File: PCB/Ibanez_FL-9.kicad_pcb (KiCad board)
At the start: 2 copper layers, 50.8 x 22.9 mm, 38 parts, among them J1 SENSOR_UART-QT, J2 PWR_IN, J6 MOTOR_OUT, M1 Feather_M4_Express, Q1 DMG2301L, U1 INA260, U2 DRV8830

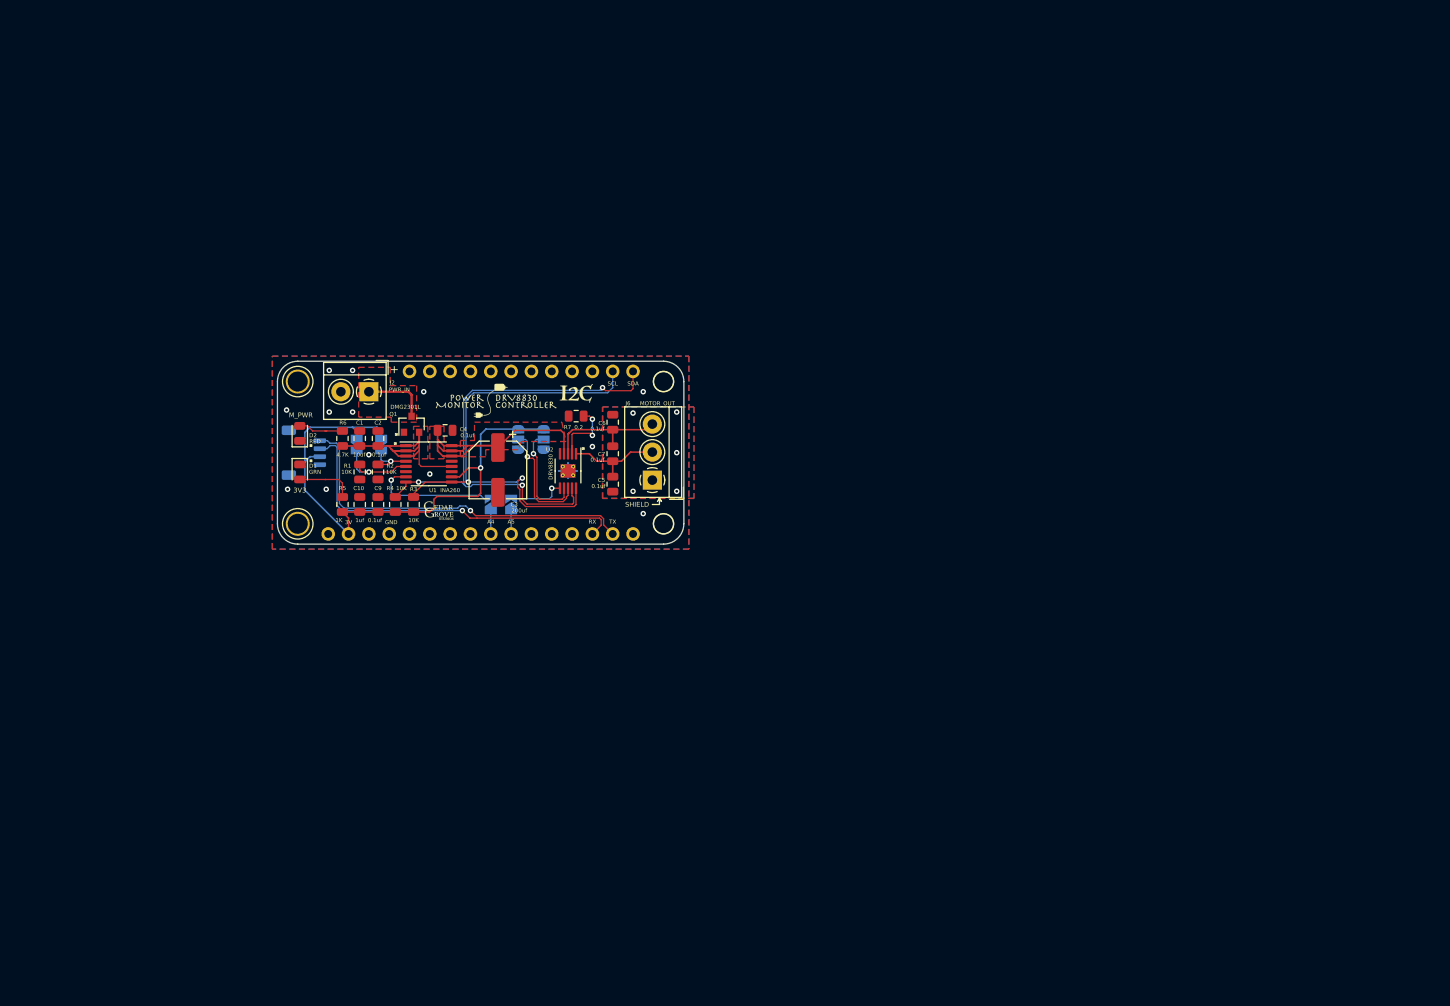
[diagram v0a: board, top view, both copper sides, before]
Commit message: update docs; correct component labels and footprints
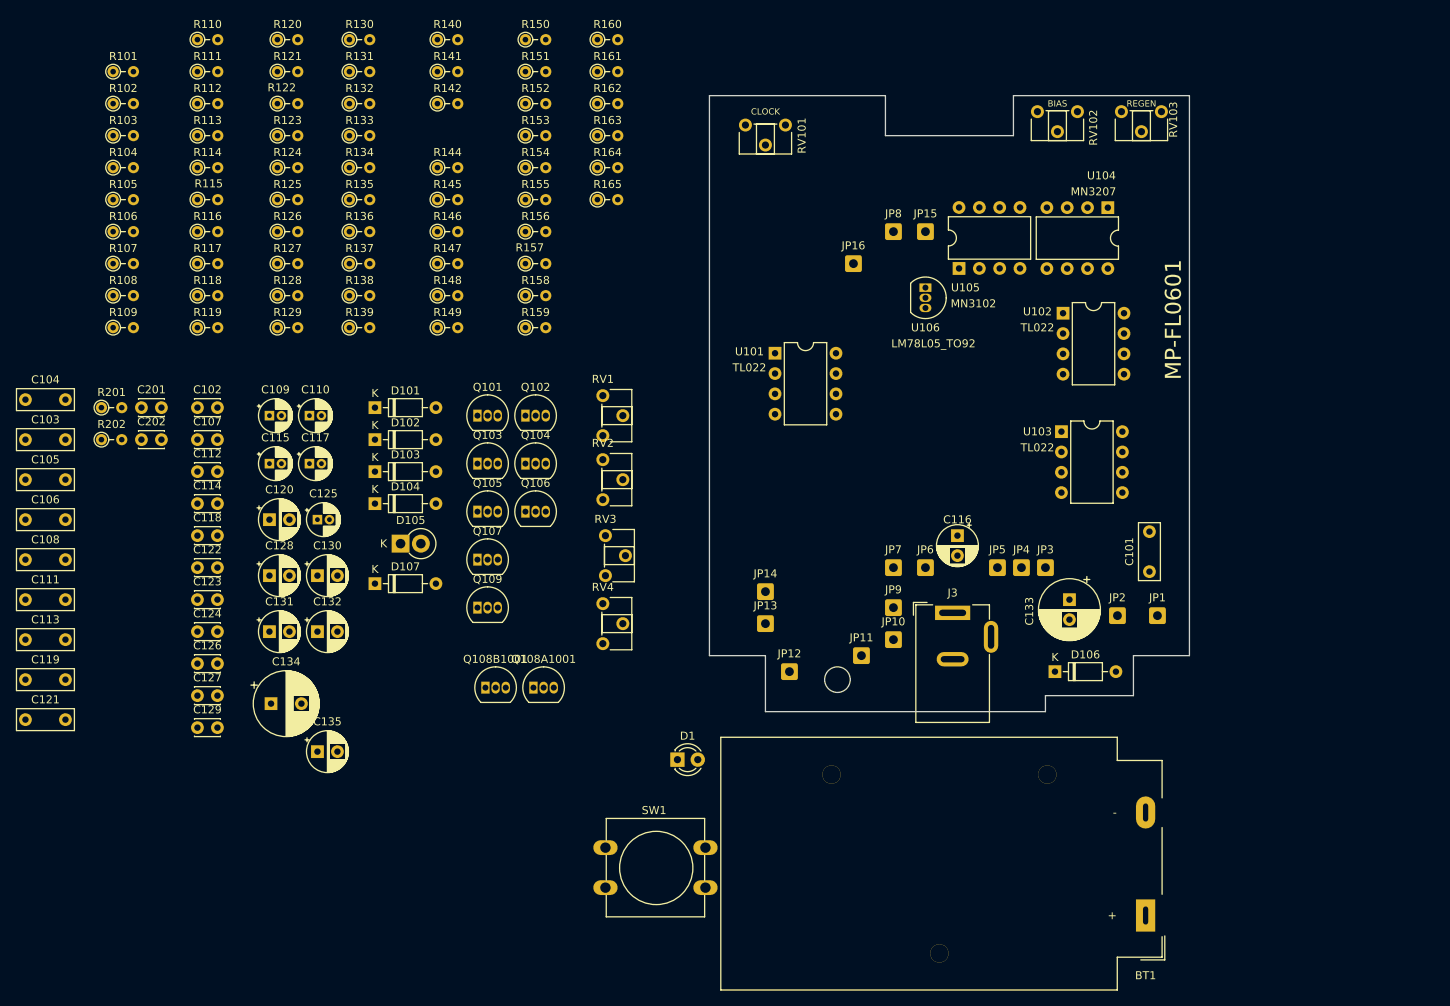
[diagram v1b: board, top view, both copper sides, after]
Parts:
- removed C1: 10uf, Capacitor_SMD:C_0805_2012Metric
- removed C10: 1uf, Capacitor_SMD:C_0805_2012Metric
- removed C2, C4, C5, C6, C7, C9: 0.1uf, Capacitor_SMD:C_0805_2012Metric
- removed C3: 200uf, Capacitor_SMD:CP_Elec_6.6x6.6
- removed D2: RED, LED_SMD:LED_0805_2012Metric
- removed G***: CedarGroveStudios_TEXT_LOGO_4x2_7mm, Adafruit:CedarGroveStudios_TEXT_LOGO_4x2_7mm
- removed G*** (x2): LOGO, Adafruit:mtc_wing_DRV8830_24x14mm
- removed G*** (x2): LOGO, Adafruit:I2C_LOGO
- removed G***: Feather_LOGO_8x4mm, Adafruit:Feather_LOGO_8x4mm
- removed G***: LOGO, Adafruit:CedarGroveStudios_TEXT_LOGO_8x5_4mm
- removed J1: SENSOR_UART-QT, Connector_JST:JST_SH_SM04B-SRSS-TB_1x04-1MP_P1.00mm_Horizontal
- removed J2: PWR_IN, TerminalBlock_4Ucon:TerminalBlock_4Ucon_1x02_P3.50mm_Horizontal
- removed J6: MOTOR_OUT, TerminalBlock_4Ucon:TerminalBlock_4Ucon_1x03_P3.50mm_Horizontal
- removed M1: Feather_M4_Express, Adafruit:Adafruit_Feather_M4_Express_bare
- removed Q1: DMG2301L, Package_TO_SOT_SMD:SOT-23
- removed R1, R2, R3, R4: 10K, Resistor_SMD:R_0805_2012Metric
- removed R5: 1K, Resistor_SMD:R_0805_2012Metric
- removed R6: 4.7K, Resistor_SMD:R_0805_2012Metric
- removed R7: 0.2, Resistor_SMD:R_0805_2012Metric
- removed U1: INA260, Package_SO:TSSOP-16_4.4x5mm_P0.65mm
- removed U2: DRV8830, Package_SO:MSOP-10-1EP_3x3mm_P0.5mm_EP1.68x1.88mm_ThermalVias
- added BT1: 9V Battery, Battery:BatteryHolder_MPD_BA9VPC_1xPP3, F.Cu at (235.5, 145.5)
- added C101: 0.047uf FILM, Capacitor_THT:C_Rect_L7.0mm_W2.5mm_P5.00mm, F.Cu at (236.0, 102.5)
- added C102: 100pf CER, Capacitor_THT:C_Disc_D3.0mm_W2.0mm_P2.50mm, F.Cu at (117.0, 82.0)
- added C103: 0.022uf FILM, Capacitor_THT:C_Rect_L7.0mm_W2.5mm_P5.00mm, F.Cu at (95.5, 86.0)
- added C104: 0.047uf FILM, Capacitor_THT:C_Rect_L7.0mm_W2.5mm_P5.00mm, F.Cu at (95.5, 81.0)
- added C105: 0.004uf FILM, Capacitor_THT:C_Rect_L7.0mm_W2.5mm_P5.00mm, F.Cu at (95.5, 91.0)
- added C106: 0.01uf FILM, Capacitor_THT:C_Rect_L7.0mm_W2.5mm_P5.00mm, F.Cu at (95.5, 96.0)
- added C107: 120pf CER, Capacitor_THT:C_Disc_D3.0mm_W2.0mm_P2.50mm, F.Cu at (117.0, 86.0)
- added C108: 0.033uf FILM, Capacitor_THT:C_Rect_L7.0mm_W2.5mm_P5.00mm, F.Cu at (95.5, 101.0)
- added C109: 1uf/50v, Capacitor_THT:CP_Radial_D4.0mm_P1.50mm, F.Cu at (126.0, 83.0)
- added C110: 1uf/50, Capacitor_THT:CP_Radial_D4.0mm_P1.50mm, F.Cu at (131.0, 83.0)
- added C111: 0.0015uf FILM, Capacitor_THT:C_Rect_L7.0mm_W2.5mm_P5.00mm, F.Cu at (95.5, 106.0)
- added C112: 0.001uf CER, Capacitor_THT:C_Disc_D3.0mm_W2.0mm_P2.50mm, F.Cu at (117.0, 90.0)
- added C113: 0.003uf FILM, Capacitor_THT:C_Rect_L7.0mm_W2.5mm_P5.00mm, F.Cu at (95.5, 111.0)
- added C114: 560pf CER, Capacitor_THT:C_Disc_D3.0mm_W2.0mm_P2.50mm, F.Cu at (117.0, 94.0)
- added C115: 1uf/50, Capacitor_THT:CP_Radial_D4.0mm_P1.50mm, F.Cu at (126.0, 89.0)
- added C116: 0.22uf/50v, Capacitor_THT:CP_Radial_D5.0mm_P2.50mm, F.Cu at (212.0, 98.0)
- added C117: 1uf/50, Capacitor_THT:CP_Radial_D4.0mm_P1.50mm, F.Cu at (131.0, 89.0)
- added C118: 100pf CER, Capacitor_THT:C_Disc_D3.0mm_W2.0mm_P2.50mm, F.Cu at (117.0, 98.0)
- added C119: 0.004 FILM, Capacitor_THT:C_Rect_L7.0mm_W2.5mm_P5.00mm, F.Cu at (95.5, 116.0)
- added C120: 10uf/16v, Capacitor_THT:CP_Radial_D5.0mm_P2.50mm, F.Cu at (126.0, 96.0)
- added C121: 0.047uf FILM, Capacitor_THT:C_Rect_L7.0mm_W2.5mm_P5.00mm, F.Cu at (95.5, 121.0)
- added C122: 1000pf CER, Capacitor_THT:C_Disc_D3.0mm_W2.0mm_P2.50mm, F.Cu at (117.0, 102.0)
- added C123: 1000pf CER, Capacitor_THT:C_Disc_D3.0mm_W2.0mm_P2.50mm, F.Cu at (117.0, 106.0)
- added C124: 1000pf CER, Capacitor_THT:C_Disc_D3.0mm_W2.0mm_P2.50mm, F.Cu at (117.0, 110.0)
- added C125: 1uf/50v, Capacitor_THT:CP_Radial_D4.0mm_P1.50mm, F.Cu at (132.0, 96.0)
- added C126: 20pf CER, Capacitor_THT:C_Disc_D3.0mm_W2.0mm_P2.50mm, F.Cu at (117.0, 114.0)
- added C127: 5pf CER, Capacitor_THT:C_Disc_D3.0mm_W2.0mm_P2.50mm, F.Cu at (117.0, 118.0)
- added C128: 22uf/10v, Capacitor_THT:CP_Radial_D5.0mm_P2.50mm, F.Cu at (126.0, 103.0)
- added C129: 0.01uf, Capacitor_THT:C_Disc_D3.0mm_W2.0mm_P2.50mm, F.Cu at (117.0, 122.0)
- added C130: 47uf/10v, Capacitor_THT:CP_Radial_D5.0mm_P2.50mm, F.Cu at (132.0, 103.0)
- added C131: 47uf/10v, Capacitor_THT:CP_Radial_D5.0mm_P2.50mm, F.Cu at (126.0, 110.0)
- added C132: 47uf/6.3v, Capacitor_THT:CP_Radial_D5.0mm_P2.50mm, F.Cu at (132.0, 110.0)
- added C133: 100uf/16v, Capacitor_THT:CP_Radial_D7.5mm_P2.50mm, F.Cu at (226.0, 106.0)
- added C134: 100uf/10v, Capacitor_THT:CP_Radial_D8.0mm_P3.80mm, F.Cu at (126.2, 119.0)
- added C135: 47uf/6.3v, Capacitor_THT:CP_Radial_D5.0mm_P2.50mm, F.Cu at (132.0, 125.0)
- added C201: 0.001uf CER, Capacitor_THT:C_Disc_D3.0mm_W2.0mm_P2.50mm, F.Cu at (110.0, 82.0)
- added C202: 0.001uf CER, Capacitor_THT:C_Disc_D3.0mm_W2.0mm_P2.50mm, F.Cu at (110.0, 86.0)
- added D101: 1N4004, Diode_THT:D_DO-35_SOD27_P7.62mm_Horizontal, F.Cu at (139.2, 82.0)
- added D102: 1N4004, Diode_THT:D_DO-35_SOD27_P7.62mm_Horizontal, F.Cu at (139.2, 86.0)
- added D103: 1N4004, Diode_THT:D_DO-35_SOD27_P7.62mm_Horizontal, F.Cu at (139.2, 90.0)
- added D104: 1N4004, Diode_THT:D_DO-35_SOD27_P7.62mm_Horizontal, F.Cu at (139.2, 94.0)
- added D105: RD5.1EB, Diode_THT:D_DO-15_P2.54mm_Vertical_KathodeUp, F.Cu at (142.4, 99.0)
- added D106: W05C, Diode_THT:D_DO-35_SOD27_P7.62mm_Horizontal, F.Cu at (224.2, 115.0)
- added D107: 1N4004, Diode_THT:D_DO-35_SOD27_P7.62mm_Horizontal, F.Cu at (139.2, 104.0)
- added J3: EXT_DC, Connector_BarrelJack:BarrelJack_Wuerth_6941xx301002, F.Cu at (211.4, 107.7)
- added JP10: BLK, Connector_Wire:SolderWire-0.5sqmm_1x01_D0.9mm_OD2.1mm, F.Cu at (204.0, 111.0)
- added JP11: W/R, Connector_Wire:SolderWire-0.5sqmm_1x01_D0.9mm_OD2.1mm, F.Cu at (200.0, 113.0)
- added JP12: PINK, Connector_Wire:SolderWire-0.5sqmm_1x01_D0.9mm_OD2.1mm, F.Cu at (191.0, 115.0)
- added JP13: GRN, Connector_Wire:SolderWire-0.5sqmm_1x01_D0.9mm_OD2.1mm, F.Cu at (188.0, 109.0)
- added JP14: ORA, Connector_Wire:SolderWire-0.5sqmm_1x01_D0.9mm_OD2.1mm, F.Cu at (188.0, 105.0)
- added JP15: RED, Connector_Wire:SolderWire-0.5sqmm_1x01_D0.9mm_OD2.1mm, F.Cu at (208.0, 60.0)
- added JP16: Y-GR, Connector_Wire:SolderWire-0.5sqmm_1x01_D0.9mm_OD2.1mm, F.Cu at (199.0, 64.0)
- added JP7: BRN, Connector_Wire:SolderWire-0.5sqmm_1x01_D0.9mm_OD2.1mm, F.Cu at (204.0, 102.0)
- added JP8: S-BL, Connector_Wire:SolderWire-0.5sqmm_1x01_D0.9mm_OD2.1mm, F.Cu at (204.0, 60.0)
- added JP9: RED, Connector_Wire:SolderWire-0.5sqmm_1x01_D0.9mm_OD2.1mm, F.Cu at (204.0, 107.0)
- added Q101: 2SC2458GR, Package_TO_SOT_THT:TO-92_Inline, F.Cu at (152.0, 83.0)
- added Q102: 2SC2458GR, Package_TO_SOT_THT:TO-92_Inline, F.Cu at (158.0, 83.0)
- added Q103: 2SK44SPC, Package_TO_SOT_THT:TO-92_Inline, F.Cu at (152.0, 89.0)
- added Q104: 2SC2458GR, Package_TO_SOT_THT:TO-92_Inline, F.Cu at (158.0, 89.0)
- added Q105: 2SC2458GR, Package_TO_SOT_THT:TO-92_Inline, F.Cu at (152.0, 95.0)
- added Q106: 2SC2458GR, Package_TO_SOT_THT:TO-92_Inline, F.Cu at (158.0, 95.0)
- added Q107: 2SA1048Y/GR, Package_TO_SOT_THT:TO-92_Inline, F.Cu at (152.0, 101.0)
- added Q108A1001: 2SC1583F, Package_TO_SOT_THT:TO-92_Inline, F.Cu at (159.0, 117.0)
- added Q108B1001: 2SC1583F, Package_TO_SOT_THT:TO-92_Inline, F.Cu at (153.0, 117.0)
- added Q109: 2SC2458GR, Package_TO_SOT_THT:TO-92_Inline, F.Cu at (152.0, 107.0)
- added R101: 1K, Resistor_THT:R_Axial_DIN0204_L3.6mm_D1.6mm_P2.54mm_Vertical, F.Cu at (106.5, 40.0)
- added R102: 510K, Resistor_THT:R_Axial_DIN0204_L3.6mm_D1.6mm_P2.54mm_Vertical, F.Cu at (106.5, 44.0)
- added R103: 91K, Resistor_THT:R_Axial_DIN0204_L3.6mm_D1.6mm_P2.54mm_Vertical, F.Cu at (106.5, 48.0)
- added R104: 18K, Resistor_THT:R_Axial_DIN0204_L3.6mm_D1.6mm_P2.54mm_Vertical, F.Cu at (106.5, 52.0)
- added R105: 180K, Resistor_THT:R_Axial_DIN0204_L3.6mm_D1.6mm_P2.54mm_Vertical, F.Cu at (106.5, 56.0)
- added R106: 510K, Resistor_THT:R_Axial_DIN0204_L3.6mm_D1.6mm_P2.54mm_Vertical, F.Cu at (106.5, 60.0)
- added R107: 100K, Resistor_THT:R_Axial_DIN0204_L3.6mm_D1.6mm_P2.54mm_Vertical, F.Cu at (106.5, 64.0)
- added R108: 10K, Resistor_THT:R_Axial_DIN0204_L3.6mm_D1.6mm_P2.54mm_Vertical, F.Cu at (106.5, 68.0)
- added R109: 47K, Resistor_THT:R_Axial_DIN0204_L3.6mm_D1.6mm_P2.54mm_Vertical, F.Cu at (106.5, 72.0)
- added R110: 12K, Resistor_THT:R_Axial_DIN0204_L3.6mm_D1.6mm_P2.54mm_Vertical, F.Cu at (117.0, 36.0)
- added R111: 12K, Resistor_THT:R_Axial_DIN0204_L3.6mm_D1.6mm_P2.54mm_Vertical, F.Cu at (117.0, 40.0)
- added R112: 10K, Resistor_THT:R_Axial_DIN0204_L3.6mm_D1.6mm_P2.54mm_Vertical, F.Cu at (117.0, 44.0)
- added R113: 100K, Resistor_THT:R_Axial_DIN0204_L3.6mm_D1.6mm_P2.54mm_Vertical, F.Cu at (117.0, 48.0)
- added R114: 5.1K, Resistor_THT:R_Axial_DIN0204_L3.6mm_D1.6mm_P2.54mm_Vertical, F.Cu at (117.0, 52.0)
- added R115: 5.1K, Resistor_THT:R_Axial_DIN0204_L3.6mm_D1.6mm_P2.54mm_Vertical, F.Cu at (117.0, 56.0)
- added R116: 56K, Resistor_THT:R_Axial_DIN0204_L3.6mm_D1.6mm_P2.54mm_Vertical, F.Cu at (117.0, 60.0)
- added R117: 18K, Resistor_THT:R_Axial_DIN0204_L3.6mm_D1.6mm_P2.54mm_Vertical, F.Cu at (117.0, 64.0)
- added R118: 18K, Resistor_THT:R_Axial_DIN0204_L3.6mm_D1.6mm_P2.54mm_Vertical, F.Cu at (117.0, 68.0)
- added R119: 18K, Resistor_THT:R_Axial_DIN0204_L3.6mm_D1.6mm_P2.54mm_Vertical, F.Cu at (117.0, 72.0)
- added R120: 10K, Resistor_THT:R_Axial_DIN0204_L3.6mm_D1.6mm_P2.54mm_Vertical, F.Cu at (127.0, 36.0)
- added R121: 13K, Resistor_THT:R_Axial_DIN0204_L3.6mm_D1.6mm_P2.54mm_Vertical, F.Cu at (127.0, 40.0)
- added R122: 13K, Resistor_THT:R_Axial_DIN0204_L3.6mm_D1.6mm_P2.54mm_Vertical, F.Cu at (127.0, 44.0)
- added R123: 10K, Resistor_THT:R_Axial_DIN0204_L3.6mm_D1.6mm_P2.54mm_Vertical, F.Cu at (127.0, 48.0)
- added R124: 100K, Resistor_THT:R_Axial_DIN0204_L3.6mm_D1.6mm_P2.54mm_Vertical, F.Cu at (127.0, 52.0)
- added R125: 100K, Resistor_THT:R_Axial_DIN0204_L3.6mm_D1.6mm_P2.54mm_Vertical, F.Cu at (127.0, 56.0)
- added R126: 51K, Resistor_THT:R_Axial_DIN0204_L3.6mm_D1.6mm_P2.54mm_Vertical, F.Cu at (127.0, 60.0)
- added R127: 91K, Resistor_THT:R_Axial_DIN0204_L3.6mm_D1.6mm_P2.54mm_Vertical, F.Cu at (127.0, 64.0)
- added R128: 18K, Resistor_THT:R_Axial_DIN0204_L3.6mm_D1.6mm_P2.54mm_Vertical, F.Cu at (127.0, 68.0)
- added R129: 91K, Resistor_THT:R_Axial_DIN0204_L3.6mm_D1.6mm_P2.54mm_Vertical, F.Cu at (127.0, 72.0)
- added R130: 10K, Resistor_THT:R_Axial_DIN0204_L3.6mm_D1.6mm_P2.54mm_Vertical, F.Cu at (136.0, 36.0)
- added R131: 470, Resistor_THT:R_Axial_DIN0204_L3.6mm_D1.6mm_P2.54mm_Vertical, F.Cu at (136.0, 40.0)
- added R132: 100K, Resistor_THT:R_Axial_DIN0204_L3.6mm_D1.6mm_P2.54mm_Vertical, F.Cu at (136.0, 44.0)
- added R133: 1M, Resistor_THT:R_Axial_DIN0204_L3.6mm_D1.6mm_P2.54mm_Vertical, F.Cu at (136.0, 48.0)
- added R134: 10K, Resistor_THT:R_Axial_DIN0204_L3.6mm_D1.6mm_P2.54mm_Vertical, F.Cu at (136.0, 52.0)
- added R135: 10K, Resistor_THT:R_Axial_DIN0204_L3.6mm_D1.6mm_P2.54mm_Vertical, F.Cu at (136.0, 56.0)
- added R136: 56K, Resistor_THT:R_Axial_DIN0204_L3.6mm_D1.6mm_P2.54mm_Vertical, F.Cu at (136.0, 60.0)
- added R137: 56K, Resistor_THT:R_Axial_DIN0204_L3.6mm_D1.6mm_P2.54mm_Vertical, F.Cu at (136.0, 64.0)
- added R138: 1M, Resistor_THT:R_Axial_DIN0204_L3.6mm_D1.6mm_P2.54mm_Vertical, F.Cu at (136.0, 68.0)
- added R139: 62K, Resistor_THT:R_Axial_DIN0204_L3.6mm_D1.6mm_P2.54mm_Vertical, F.Cu at (136.0, 72.0)
- added R140: 22K, Resistor_THT:R_Axial_DIN0204_L3.6mm_D1.6mm_P2.54mm_Vertical, F.Cu at (147.0, 36.0)
- added R141: 22, Resistor_THT:R_Axial_DIN0204_L3.6mm_D1.6mm_P2.54mm_Vertical, F.Cu at (147.0, 40.0)
- added R142: 100, Resistor_THT:R_Axial_DIN0204_L3.6mm_D1.6mm_P2.54mm_Vertical, F.Cu at (147.0, 44.0)
- added R144: 2.2K, Resistor_THT:R_Axial_DIN0204_L3.6mm_D1.6mm_P2.54mm_Vertical, F.Cu at (147.0, 52.0)
- added R145: 330, Resistor_THT:R_Axial_DIN0204_L3.6mm_D1.6mm_P2.54mm_Vertical, F.Cu at (147.0, 56.0)
- added R146: 33K, Resistor_THT:R_Axial_DIN0204_L3.6mm_D1.6mm_P2.54mm_Vertical, F.Cu at (147.0, 60.0)
- added R147: 27K, Resistor_THT:R_Axial_DIN0204_L3.6mm_D1.6mm_P2.54mm_Vertical, F.Cu at (147.0, 64.0)
- added R148: 10K, Resistor_THT:R_Axial_DIN0204_L3.6mm_D1.6mm_P2.54mm_Vertical, F.Cu at (147.0, 68.0)
- added R149: 9.1K, Resistor_THT:R_Axial_DIN0204_L3.6mm_D1.6mm_P2.54mm_Vertical, F.Cu at (147.0, 72.0)
- added R150: 2.2M, Resistor_THT:R_Axial_DIN0204_L3.6mm_D1.6mm_P2.54mm_Vertical, F.Cu at (158.0, 36.0)
- added R151: 150K, Resistor_THT:R_Axial_DIN0204_L3.6mm_D1.6mm_P2.54mm_Vertical, F.Cu at (158.0, 40.0)
- added R152: 220K, Resistor_THT:R_Axial_DIN0204_L3.6mm_D1.6mm_P2.54mm_Vertical, F.Cu at (158.0, 44.0)
- added R153: 200K, Resistor_THT:R_Axial_DIN0204_L3.6mm_D1.6mm_P2.54mm_Vertical, F.Cu at (158.0, 48.0)
- added R154: 100K, Resistor_THT:R_Axial_DIN0204_L3.6mm_D1.6mm_P2.54mm_Vertical, F.Cu at (158.0, 52.0)
- added R155: 62K, Resistor_THT:R_Axial_DIN0204_L3.6mm_D1.6mm_P2.54mm_Vertical, F.Cu at (158.0, 56.0)
- added R156: 51K, Resistor_THT:R_Axial_DIN0204_L3.6mm_D1.6mm_P2.54mm_Vertical, F.Cu at (158.0, 60.0)
- added R157: 1.2K, Resistor_THT:R_Axial_DIN0204_L3.6mm_D1.6mm_P2.54mm_Vertical, F.Cu at (158.0, 64.0)
- added R158: 10K, Resistor_THT:R_Axial_DIN0204_L3.6mm_D1.6mm_P2.54mm_Vertical, F.Cu at (158.0, 68.0)
- added R159: 10K, Resistor_THT:R_Axial_DIN0204_L3.6mm_D1.6mm_P2.54mm_Vertical, F.Cu at (158.0, 72.0)
- added R160: 110K, Resistor_THT:R_Axial_DIN0204_L3.6mm_D1.6mm_P2.54mm_Vertical, F.Cu at (167.0, 36.0)
- added R161: 100K, Resistor_THT:R_Axial_DIN0204_L3.6mm_D1.6mm_P2.54mm_Vertical, F.Cu at (167.0, 40.0)
- added R162: 270K, Resistor_THT:R_Axial_DIN0204_L3.6mm_D1.6mm_P2.54mm_Vertical, F.Cu at (167.0, 44.0)
- added R163: 10K, Resistor_THT:R_Axial_DIN0204_L3.6mm_D1.6mm_P2.54mm_Vertical, F.Cu at (167.0, 48.0)
- added R164: 10K, Resistor_THT:R_Axial_DIN0204_L3.6mm_D1.6mm_P2.54mm_Vertical, F.Cu at (167.0, 52.0)
- added R165: 4.7K, Resistor_THT:R_Axial_DIN0204_L3.6mm_D1.6mm_P2.54mm_Vertical, F.Cu at (167.0, 56.0)
- added R201: 100K, Resistor_THT:R_Axial_DIN0204_L3.6mm_D1.6mm_P2.54mm_Vertical, F.Cu at (105.0, 82.0)
- added R202: 100K, Resistor_THT:R_Axial_DIN0204_L3.6mm_D1.6mm_P2.54mm_Vertical, F.Cu at (105.0, 86.0)
- added REF**: MountingHole_3.2mm_M3, MountingHole:MountingHole_3.2mm_M3, F.Cu at (197.0, 116.0)
- added RV1: 500K, Potentiometer_THT:Potentiometer_ACP_CA6-H2,5_Horizontal, F.Cu at (167.7, 80.5)
- added RV101: 20K, Potentiometer_THT:Potentiometer_ACP_CA6-H2,5_Horizontal, F.Cu at (190.5, 46.7)
- added RV102: 10K, Potentiometer_THT:Potentiometer_ACP_CA6-H2,5_Horizontal, F.Cu at (227.0, 45.0)
- added RV103: 100K, Potentiometer_THT:Potentiometer_ACP_CA6-H2,5_Horizontal, F.Cu at (237.5, 45.0)
- added RV2: 100K, Potentiometer_THT:Potentiometer_ACP_CA6-H2,5_Horizontal, F.Cu at (167.7, 88.5)
- added RV3: 50K, Potentiometer_THT:Potentiometer_ACP_CA6-H2,5_Horizontal, F.Cu at (168.0, 98.0)
- added RV4: 10K, Potentiometer_THT:Potentiometer_ACP_CA6-H2,5_Horizontal, F.Cu at (167.7, 106.5)
- added SW1: NORMAL/EFFECT, Button_Switch_THT:SW_PUSH-12mm, F.Cu at (168.0, 137.0)
- added U101: TL022, Package_DIP:DIP-8_W7.62mm, F.Cu at (189.2, 75.2)
- added U102: TL022, Package_DIP:DIP-8_W7.62mm, F.Cu at (225.2, 70.2)
- added U103: TL022, Package_DIP:DIP-8_W7.62mm, F.Cu at (225.0, 85.0)
- added U104: MN3207, Package_DIP:DIP-8_W7.62mm, F.Cu at (230.8, 57.0)
- added U105: MN3102, Package_DIP:DIP-8_W7.62mm, F.Cu at (212.2, 64.6)
- added U106: LM78L05_TO92, Package_TO_SOT_THT:TO-92_Inline, F.Cu at (208.0, 67.0)
- D1: value GRN -> LN21CPSL; footprint LED_SMD:LED_0805_2012Metric -> LED_THT:LED_D3.0mm_Clear
- JP1: value C_A0 -> GRY; footprint Jumper:SolderJumper-2_P1.3mm_Open_TrianglePad1.0x1.5mm -> Connector_Wire:SolderWire-0.5sqmm_1x01_D0.9mm_OD2.1mm; moved to F.Cu
- JP2: value C_A1 -> YEL; footprint Jumper:SolderJumper-2_P1.3mm_Open_TrianglePad1.0x1.5mm -> Connector_Wire:SolderWire-0.5sqmm_1x01_D0.9mm_OD2.1mm; moved to F.Cu
- JP3: value C_ALERT_A4 -> WHT; footprint Jumper:SolderJumper-2_P1.3mm_Open_TrianglePad1.0x1.5mm -> Connector_Wire:SolderWire-0.5sqmm_1x01_D0.9mm_OD2.1mm; moved to F.Cu
- JP4: value M_A0 -> RED; footprint Jumper:SolderJumper-3_P1.3mm_Open_RoundedPad1.0x1.5mm -> Connector_Wire:SolderWire-0.5sqmm_1x01_D0.9mm_OD2.1mm; moved to F.Cu
- JP5: value M_FAULT_A5 -> BLU; footprint Jumper:SolderJumper-2_P1.3mm_Open_TrianglePad1.0x1.5mm -> Connector_Wire:SolderWire-0.5sqmm_1x01_D0.9mm_OD2.1mm; moved to F.Cu
- JP6: value M_A1 -> PUR; footprint Jumper:SolderJumper-3_P1.3mm_Open_RoundedPad1.0x1.5mm -> Connector_Wire:SolderWire-0.5sqmm_1x01_D0.9mm_OD2.1mm; moved to F.Cu
- moved JP1 102.4 mm to (237.0, 108.0), turned to 0 degrees
- moved JP2 94.5 mm to (232.0, 108.0), turned to 0 degrees
- moved JP3 69.8 mm to (223.0, 102.0), turned to 0 degrees
- moved JP4 61.8 mm to (220.0, 102.0), turned to 0 degrees
- moved JP5 61.3 mm to (217.0, 102.0), turned to 0 degrees
- moved D1 59.3 mm to (177.0, 126.0), turned to 0 degrees
- moved JP6 53.4 mm to (208.0, 102.0), turned to 0 degrees
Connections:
- D1 pad 1: GND -> Net-(D1-Pad1)
- JP1 pad 1: +3V3 -> Net-(JP1-Pad1)
- JP2 pad 1: +3V3 -> Net-(JP2-Pad1)
- JP3 pad 1: /C_ALERT -> Net-(JP3-Pad1)
- JP4 pad 1: GND -> Net-(JP4-Pad1)
- JP5 pad 1: /M_FAULT -> Net-(C116-Pad2)
- JP6 pad 1: GND -> Net-(JP6-Pad1)
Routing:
- net +3V3: track 72.0 -> 0.00 mm, vias 1 -> 0
- net /SDA: track 63.9 -> 0.00 mm, vias 3 -> 0
- net /SCL: track 58.9 -> 0.00 mm, vias 2 -> 0
- net /SENSOR_TX: track 46.3 -> 0.00 mm, vias 1 -> 0
- net /SENSOR_RX: track 45.7 -> 0.00 mm, vias 1 -> 0
- net /M_PWR_IN: track 31.9 -> 0.00 mm
- net /C_PWR_IN: track 27.8 -> 0.00 mm
- net Net-(JP3-Pad2): track 16.3 -> 0.00 mm, vias 1 -> 0
- net /M_OUT_1: track 15.7 -> 0.00 mm
- net Net-(JP6-Pad2): track 14.6 -> 0.00 mm, vias 1 -> 0
- net Net-(JP4-Pad2): track 13.1 -> 0.00 mm, vias 1 -> 0
- net /M_OUT_2: track 12.3 -> 0.00 mm
- net Net-(JP1-Pad2): track 10.9 -> 0.00 mm, vias 1 -> 0
- net Net-(R7-Pad2): track 9.42 -> 0.00 mm, vias 2 -> 0
- net /PWR_IN: track 8.17 -> 0.00 mm
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- removed copper zone on F.Cu, net /C_PWR_IN
- removed copper zone on F.Cu, net /M_PWR_IN
- removed copper zone on B.Cu, net /M_SHIELD
- removed copper zone on F.Cu, net /M_SHIELD
- removed copper zone on F.Cu, net /PWR_IN
- removed copper zone on B.Cu, net GND
- removed copper zone on F.Cu, net GND
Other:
- board size 50.8 x 22.9 mm -> 60 x 77 mm
- board text added: "JP1"
- board text added: "JP10"
- board text added: "JP11"
- board text added: "JP12"
- board text added: "JP13"
- board text added: "JP14"
- board text added: "JP15"
- board text added: "JP16"
- board text added: "JP2"
- board text added: "JP3"
- board text added: "JP4"
- board text added: "JP5"
- board text added: "JP6"
- board text added: "JP7"
- board text added: "JP8"
- board text added: "JP9"
- board text added: "MAXON MP-FL0601"
- board text added: "MP-FL0601"
- board text added: "U104 MN3207"
- board text added: "U105 MN3102"
- board text removed: "+"
- board text removed: "3V3"
- board text removed: "CURRENT"
- board text removed: "CURRENT MONITOR I2C ADDRESS (0x40)"
- board text removed: "FAULT STATUS"
- board text removed: "GND"
- board text removed: "HI"
- board text removed: "LO"
- board text removed: "MOTOR"
- board text removed: "MOTOR CONTROLLER I2C ADRESS (0x60): A0 and A1 Low"
- board text removed: "M_PWR"
- board text removed: "Motor_Tester_DRV8830_Wing v01 2021-08-29"
- board text removed: "OPEN"
- board text removed: "RX"
- board text removed: "SHIELD"
- board text removed: "TX"

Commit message: update docs
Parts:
- moved U101 37.4 mm to (225.2, 85.2)
- moved U103 37.1 mm to (189.2, 75.2)
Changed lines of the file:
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@@
   )
   (footprint "Package_DIP:DIP-8_W7.62mm" (layer "F.Cu")
-    (at 189.2 75.2)
+    (at 225.2 85.2)
     (descr "8-lead though-hole mounted DIP package, row spacing 7.62 mm (300 mils)")
     (tags "THT DIP DIL PDIP 2.54mm 7.62mm 300mil")
@@
   )
   (footprint "Package_DIP:DIP-8_W7.62mm" (layer "F.Cu")
-    (at 225 85)
+    (at 189.2 75.2)
     (descr "8-lead though-hole mounted DIP package, row spacing 7.62 mm (300 mils)")
     (tags "THT DIP DIL PDIP 2.54mm 7.62mm 300mil")

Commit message: update pcb layout
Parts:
- moved C110 88.1 mm to (218.3, 71.0)
- moved JP15 6.80 mm to (201.5, 58.0)
- moved JP16 6.80 mm to (192.5, 62.0)
- moved JP8 6.80 mm to (197.5, 58.0)
- moved U106 6.26 mm to (202.6, 70.2)
- moved U105 5.83 mm to (207.2, 61.6)
- moved U104 5.41 mm to (226.3, 54.0)
- moved J3 3.16 mm to (210.4, 104.7)
- moved REF** 3.16 mm to (196.0, 113.0)
- moved RV101 3.07 mm to (192.0, 44.0)
- moved RV103 1.80 mm to (236.0, 44.0)
- moved RV102 1.12 mm to (226.5, 44.0)
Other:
- board text removed: "JP1"
- board text removed: "JP10"
- board text removed: "JP11"
- board text removed: "JP12"
- board text removed: "JP13"
- board text removed: "JP14"
- board text removed: "JP15"
- board text removed: "JP16"
- board text removed: "JP2"
- board text removed: "JP3"
- board text removed: "JP4"
- board text removed: "JP5"
- board text removed: "JP6"
- board text removed: "JP7"
- board text removed: "JP8"
- board text removed: "JP9"
- board text removed: "U104 MN3207"
- board text removed: "U105 MN3102"

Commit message: update pcb layout
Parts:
- C101: footprint Capacitor_THT:C_Rect_L7.0mm_W2.5mm_P5.00mm -> Capacitor_THT:C_Rect_L7.2mm_W3.5mm_P5.00mm_FKS2_FKP2_MKS2_MKP2
- C104: footprint Capacitor_THT:C_Rect_L7.0mm_W2.5mm_P5.00mm -> Capacitor_THT:C_Rect_L7.0mm_W2.0mm_P5.00mm
- C133: footprint Capacitor_THT:CP_Radial_D7.5mm_P2.50mm -> Capacitor_THT:CP_Radial_D6.3mm_P2.50mm
- C134: footprint Capacitor_THT:CP_Radial_D8.0mm_P3.80mm -> Capacitor_THT:CP_Radial_D5.0mm_P2.00mm
- D101, D102: footprint Diode_THT:D_DO-35_SOD27_P7.62mm_Horizontal -> Diode_THT:D_T-1_P2.54mm_Vertical_KathodeUp
- moved C104 141.5 mm to (237.0, 78.5), turned to 180 degrees
- moved R105 132.1 mm to (236.2, 81.0), turned to 180 degrees
- moved R109 129.8 mm to (236.2, 76.0), turned to 180 degrees
- moved R108 127.9 mm to (234.2, 74.0), turned to 180 degrees
- moved R107 124.6 mm to (231.0, 68.5), turned to -90 degrees
- moved D102 98.5 mm to (236.5, 70.9), turned to 90 degrees
- moved D101 95.3 mm to (233.5, 68.6), turned to -90 degrees
- moved C134 83.3 mm to (185.0, 60.0), turned to -90 degrees
- moved U106 9.01 mm to (203.1, 61.2)
- moved C135 7.21 mm to (126.0, 121.0)
- moved C110 6.92 mm to (213.5, 66.0)
- moved U102 5.94 mm to (221.0, 66.0)
- moved JP11 5.85 mm to (198.0, 107.5)
- moved U101 5.28 mm to (221.0, 82.0)
- moved U103 5.20 mm to (189.2, 70.0)
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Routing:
- net Net-(C104-Pad2): track 0.00 -> 11.7 mm
- net /CP5: track 0.00 -> 8.01 mm
- net /CP4: track 0.00 -> 7.89 mm
- net Net-(D101-Pad2): track 0.00 -> 6.27 mm
- net Net-(C104-Pad1): track 0.00 -> 2.82 mm

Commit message: update pcb layout
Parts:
- C108: footprint Capacitor_THT:C_Rect_L7.0mm_W2.5mm_P5.00mm -> Capacitor_THT:C_Rect_L7.0mm_W2.0mm_P5.00mm
- C128: value 22uf/10v -> 22uf/10v TAN; footprint Capacitor_THT:CP_Radial_D5.0mm_P2.50mm -> Capacitor_THT:CP_Radial_Tantal_D4.5mm_P5.00mm
- moved C108 143.5 mm to (230.0, 51.0), turned to 180 degrees
- moved C106 142.7 mm to (233.5, 59.5), turned to 90 degrees
- moved C107 122.0 mm to (234.0, 51.5), turned to 90 degrees
- moved R112 115.1 mm to (232.0, 48.5), turned to -90 degrees
- moved C126 113.9 mm to (212.2, 51.5), turned to 180 degrees
- moved C127 113.4 mm to (206.2, 48.0), turned to 180 degrees
- moved R115 113.0 mm to (229.7, 48.5), turned to 180 degrees
- moved R113 106.0 mm to (223.0, 49.3), turned to -90 degrees
- moved C125 98.5 mm to (219.5, 50.7), turned to 90 degrees
- moved C109 96.3 mm to (215.7, 48.0), turned to 180 degrees
- moved R114 94.4 mm to (211.2, 47.0), turned to 180 degrees
- moved C128 90.6 mm to (198.0, 48.0), turned to 90 degrees
- moved Q101 83.1 mm to (230.1, 54.7), turned to -90 degrees
- moved Q107 65.8 mm to (197.9, 53.8), turned to 90 degrees
- moved R146 59.0 mm to (205.2, 50.5), turned to 180 degrees
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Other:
- board text added: "CP1"
- board text added: "CP11"
- board text added: "CP15"
- board text added: "CP4"
- board text added: "CP5"
- board text added: "CP7"
- board text added: "CP8"
- board text added: "CP9"

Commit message: update pcb layout
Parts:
- C103, C105: footprint Capacitor_THT:C_Rect_L7.0mm_W2.5mm_P5.00mm -> Capacitor_THT:C_Rect_L7.0mm_W2.0mm_P5.00mm
- D103, D104, D107: footprint Diode_THT:D_DO-35_SOD27_P7.62mm_Horizontal -> Diode_THT:D_T-1_P2.54mm_Vertical_KathodeUp
- moved C105 141.5 mm to (237.0, 88.5), turned to 90 degrees
- moved R101 138.9 mm to (235.0, 92.7), turned to 90 degrees
- moved R102 131.8 mm to (229.2, 92.0), turned to 180 degrees
- moved C103 131.5 mm to (226.5, 94.0)
- moved R104 131.4 mm to (232.0, 90.7), turned to 90 degrees
- moved R103 130.8 mm to (231.5, 86.2), turned to 90 degrees
- moved R110 120.2 mm to (233.5, 65.7), turned to 90 degrees
- moved C102 117.1 mm to (234.0, 86.2), turned to 90 degrees
- moved R111 116.5 mm to (231.5, 61.5)
- moved R116 106.4 mm to (223.3, 64.0)
- moved C135 105.5 mm to (229.2, 99.0), turned to 180 degrees
- moved R130 101.6 mm to (220.8, 92.0)
- moved R131 100.8 mm to (218.8, 97.5)
- moved R132 97.6 mm to (219.0, 95.5)
- moved C120 87.8 mm to (213.8, 96.0)
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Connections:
- C120 pad 2: Net-(C120-Pad2) -> Net-(R131-Pad1)
- R101 pad 1: Net-(R101-Pad1) -> Net-(C101-Pad2)
- R101 pad 2: Net-(C101-Pad2) -> Net-(R101-Pad2)
- R102 pad 1: /4.5v -> Net-(R101-Pad2)
- R102 pad 2: Net-(R101-Pad1) -> /4.5v
- R103 pad 1: /CP4 -> Net-(C102-Pad1)
- R103 pad 2: Net-(C102-Pad1) -> /CP4
- R104 pad 1: Net-(C102-Pad1) -> Net-(C105-Pad2)
- R104 pad 2: Net-(C105-Pad2) -> Net-(C102-Pad1)
- R105 pad 1: Net-(C104-Pad1) -> /CP4
- R105 pad 2: /CP4 -> Net-(C104-Pad1)
- R108 pad 1: Net-(D101-Pad2) -> Net-(C104-Pad2)
- R108 pad 2: Net-(C104-Pad2) -> Net-(D101-Pad2)
- R109 pad 1: Net-(R109-Pad1) -> Net-(C104-Pad2)
- R109 pad 2: Net-(C104-Pad2) -> Net-(RV103-Pad1)
- R110 pad 1: Net-(C106-Pad1) -> /CP5
- R110 pad 2: /CP5 -> Net-(C106-Pad1)
- R114 pad 1: Net-(R114-Pad1) -> +5V
- R114 pad 2: +5V -> Net-(RV102-Pad1)
- R115 pad 1: GND -> Net-(RV102-Pad3)
- R115 pad 2: Net-(R115-Pad2) -> GND
- R130 pad 1: /4.5v -> Net-(U101-Pad3)
- R130 pad 2: Net-(R130-Pad2) -> /4.5v
- R131 pad 1: Net-(JP3-Pad1) -> Net-(R131-Pad1)
- R131 pad 2: Net-(C120-Pad2) -> Net-(JP3-Pad1)
- R145 pad 1: Net-(Q107-Pad2) -> /CP9
- R145 pad 2: /CP9 -> Net-(Q107-Pad2)
- R147 pad 1: Net-(C127-Pad2) -> +5V
- R147 pad 2: +5V -> Net-(C127-Pad2)
- RV102 pad 1: Net-(R114-Pad1) -> Net-(RV102-Pad1)
- RV102 pad 3: Net-(R115-Pad2) -> Net-(RV102-Pad3)
- RV103 pad 1: Net-(R109-Pad1) -> Net-(RV103-Pad1)
- U101 pad 3: Net-(R130-Pad2) -> Net-(U101-Pad3)
- U101 pad 5: Net-(R101-Pad1) -> Net-(R101-Pad2)
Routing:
- net Net-(C104-Pad2): track 11.7 -> 0.00 mm
- net /CP5: track 8.01 -> 0.00 mm
- net /CP4: track 7.89 -> 0.00 mm
- net Net-(D101-Pad2): track 6.27 -> 0.00 mm
- net Net-(C104-Pad1): track 2.82 -> 0.00 mm
